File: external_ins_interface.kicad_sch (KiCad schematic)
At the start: 7 parts, among them J15 Conn_01x04, U2 MAX3232EETE+

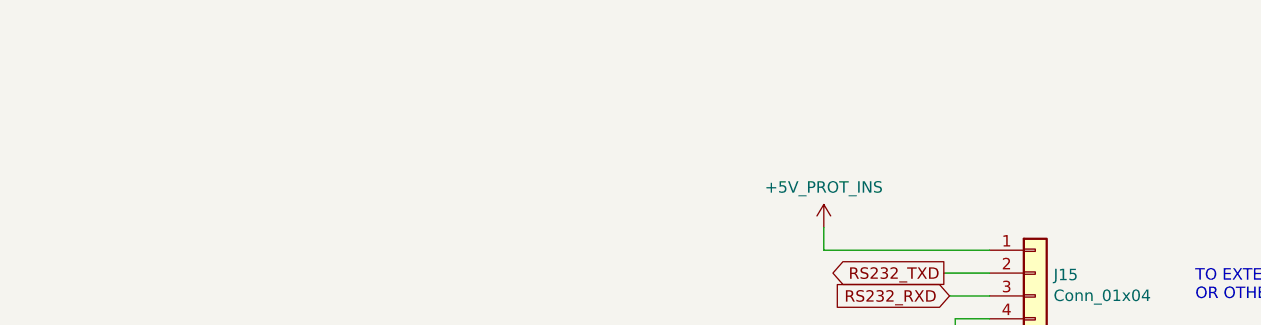
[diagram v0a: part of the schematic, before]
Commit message: change vectornav schematic naming for clarity
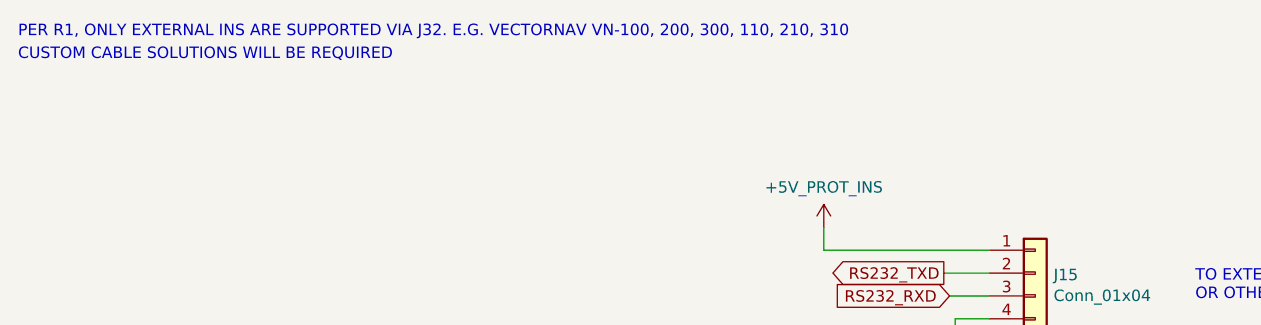
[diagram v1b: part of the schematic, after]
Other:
- note added: "CUSTOM CABLE SOLUTIONS WILL BE REQUIRED"
- note added: "PER R1, ONLY EXTERNAL INS ARE SUPPORTED VIA J32. E.G. VECTORNAV VN-100, 200, 300, 110, 210, 310"
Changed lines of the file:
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@@
   (title_block
     (title "EchoPilot Carrier")
+    (date "2023-06-25")
+    (rev "1")
     (company "Echo MAV, LLC")
   )
@@
     (effects (font (size 1.27 1.27)) (justify left bottom))
   )
+  (text "PER R1, ONLY EXTERNAL INS ARE SUPPORTED VIA J32. E.G. VECTORNAV VN-100, 200, 300, 110, 210, 310"
+    (at 29.845 26.67 0)
+    (effects (font (size 1.27 1.27)) (justify left bottom))
+  )
+  (text "CUSTOM CABLE SOLUTIONS WILL BE REQUIRED" (at 29.845 29.21 0)
+    (effects (font (size 1.27 1.27)) (justify left bottom))
+  )
   (text "TO EXTERNAL INS\nOR OTHER RS-232 DEVICE" (at 160.655 55.88 0)
     (effects (font (size 1.27 1.27)) (justify left bottom))
@@
         )
       )
-      (project "pixc4-jetson-universal-carrier"
+      (project "echopilot_ai_carrier"
         (path "/c1cd829b-ce6d-45d4-ac65-d2dab15a61f6/166856f5-4c9d-451e-956d-2d8dfacdfe56"
           (reference "C40") (unit 1)
@@
     (pin "1")
     (instances
-      (project "pixc4-jetson-universal-carrier"
+      (project "echopilot_ai_carrier"
         (path "/c1cd829b-ce6d-45d4-ac65-d2dab15a61f6/166856f5-4c9d-451e-956d-2d8dfacdfe56"
           (reference "#PWR055") (unit 1)
@@
         )
       )
-      (project "pixc4-jetson-universal-carrier"
+      (project "echopilot_ai_carrier"
         (path "/c1cd829b-ce6d-45d4-ac65-d2dab15a61f6/166856f5-4c9d-451e-956d-2d8dfacdfe56"
           (reference "C36") (unit 1)
@@
         )
       )
-      (project "pixc4-jetson-universal-carrier"
+      (project "echopilot_ai_carrier"
         (path "/c1cd829b-ce6d-45d4-ac65-d2dab15a61f6/166856f5-4c9d-451e-956d-2d8dfacdfe56"
           (reference "#PWR0151") (unit 1)
@@
     (pin "4")
     (instances
-      (project "pixc4-jetson-universal-carrier"
+      (project "echopilot_ai_carrier"
         (path "/c1cd829b-ce6d-45d4-ac65-d2dab15a61f6/00000000-0000-0000-0000-0000637b8ac9"
           (reference "J15") (unit 1)
@@
         )
       )
-      (project "pixc4-jetson-universal-carrier"
+      (project "echopilot_ai_carrier"
         (path "/c1cd829b-ce6d-45d4-ac65-d2dab15a61f6/166856f5-4c9d-451e-956d-2d8dfacdfe56"
           (reference "#PWR0146") (unit 1)
@@
         )
       )
-      (project "pixc4-jetson-universal-carrier"
+      (project "echopilot_ai_carrier"
         (path "/c1cd829b-ce6d-45d4-ac65-d2dab15a61f6/166856f5-4c9d-451e-956d-2d8dfacdfe56"
           (reference "#PWR0150") (unit 1)
@@
     (pin "1")
     (instances
-      (project "pixc4-jetson-universal-carrier"
+      (project "echopilot_ai_carrier"
         (path "/c1cd829b-ce6d-45d4-ac65-d2dab15a61f6/00000000-0000-0000-0000-0000637b8aa2"
           (reference "#PWR0111") (unit 1)
@@
         )
       )
-      (project "pixc4-jetson-universal-carrier"
+      (project "echopilot_ai_carrier"
         (path "/c1cd829b-ce6d-45d4-ac65-d2dab15a61f6/166856f5-4c9d-451e-956d-2d8dfacdfe56"
           (reference "C37") (unit 1)
@@
         )
       )
-      (project "pixc4-jetson-universal-carrier"
+      (project "echopilot_ai_carrier"
         (path "/c1cd829b-ce6d-45d4-ac65-d2dab15a61f6/166856f5-4c9d-451e-956d-2d8dfacdfe56"
           (reference "C39") (unit 1)
@@
         )
       )
-      (project "pixc4-jetson-universal-carrier"
+      (project "echopilot_ai_carrier"
         (path "/c1cd829b-ce6d-45d4-ac65-d2dab15a61f6/166856f5-4c9d-451e-956d-2d8dfacdfe56"
           (reference "C38") (unit 1)
@@
     (pin "1")
     (instances
-      (project "pixc4-jetson-universal-carrier"
+      (project "echopilot_ai_carrier"
         (path "/c1cd829b-ce6d-45d4-ac65-d2dab15a61f6/166856f5-4c9d-451e-956d-2d8dfacdfe56"
           (reference "#PWR0239") (unit 1)
@@
         )
       )
-      (project "pixc4-jetson-universal-carrier"
+      (project "echopilot_ai_carrier"
         (path "/c1cd829b-ce6d-45d4-ac65-d2dab15a61f6/166856f5-4c9d-451e-956d-2d8dfacdfe56"
           (reference "#PWR0149") (unit 1)
@@
         )
       )
-      (project "pixc4-jetson-universal-carrier"
+      (project "echopilot_ai_carrier"
         (path "/c1cd829b-ce6d-45d4-ac65-d2dab15a61f6/166856f5-4c9d-451e-956d-2d8dfacdfe56"
           (reference "U7") (unit 1)

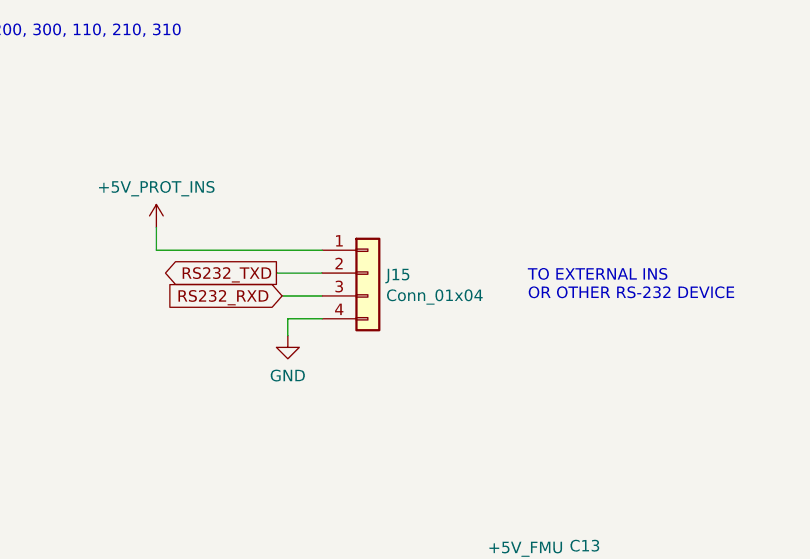
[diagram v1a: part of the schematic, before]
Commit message: updates for Rev1B boards, pinout changes on J5 and J8
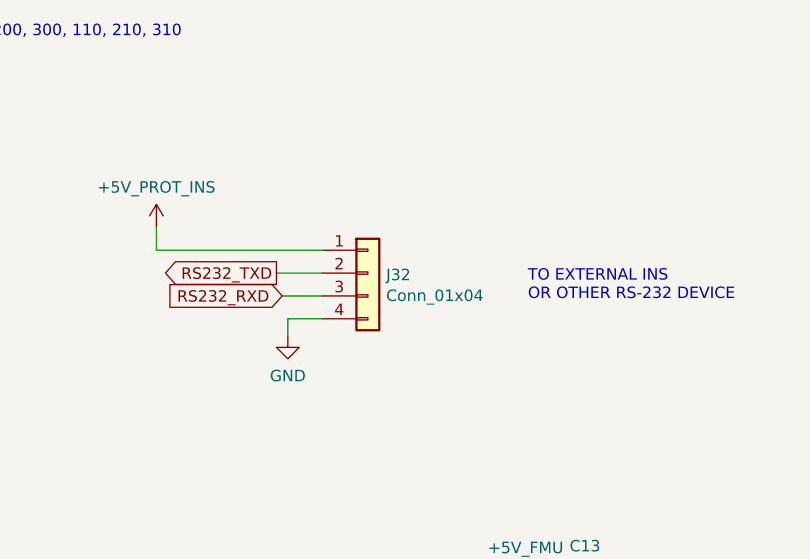
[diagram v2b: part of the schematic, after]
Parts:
- renumbered J15 to J32
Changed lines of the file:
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@@
   (symbol (lib_id "Connector_Generic:Conn_01x04") (at 142.875 52.705 0) (unit 1)
     (in_bom yes) (on_board yes) (dnp no)
-    (property "Reference" "J15" (at 144.907 52.9082 0)
+    (property "Reference" "J32" (at 144.907 52.9082 0)
       (effects (font (size 1.27 1.27)) (justify left))
     )
@@
     (instances
       (project "echopilot_ai_carrier"
-        (path "/c1cd829b-ce6d-45d4-ac65-d2dab15a61f6/00000000-0000-0000-0000-0000637b8ac9"
-          (reference "J15") (unit 1)
-        )
         (path "/c1cd829b-ce6d-45d4-ac65-d2dab15a61f6/166856f5-4c9d-451e-956d-2d8dfacdfe56"
           (reference "J32") (unit 1)
@@
   (symbol (lib_id "archangel:+5V_FMU") (at 160.02 87.63 0) (unit 1)
     (in_bom yes) (on_board yes) (dnp no)
-    (property "Reference" "#PWR0111" (at 160.02 91.44 0)
+    (property "Reference" "#PWR0147" (at 160.02 91.44 0)
       (effects (font (size 1.27 1.27)) hide)
     )
@@
     (instances
       (project "echopilot_ai_carrier"
-        (path "/c1cd829b-ce6d-45d4-ac65-d2dab15a61f6/00000000-0000-0000-0000-0000637b8aa2"
-          (reference "#PWR0111") (unit 1)
-        )
         (path "/c1cd829b-ce6d-45d4-ac65-d2dab15a61f6/166856f5-4c9d-451e-956d-2d8dfacdfe56"
           (reference "#PWR0147") (unit 1)
